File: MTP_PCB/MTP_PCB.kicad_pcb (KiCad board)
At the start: 2 copper layers, 65 x 56 mm, 21 parts, among them J1 GPIO, J2 USB_A, J3 Conn_01x03, SW1 SW_DPDT_x2, SW2 SW_DPDT_x2, SW3 SW_DPDT_x2, SW4 SW_DIP_x01, SW6 SW_DIP_x01, U1 NRF24L01_Breakout

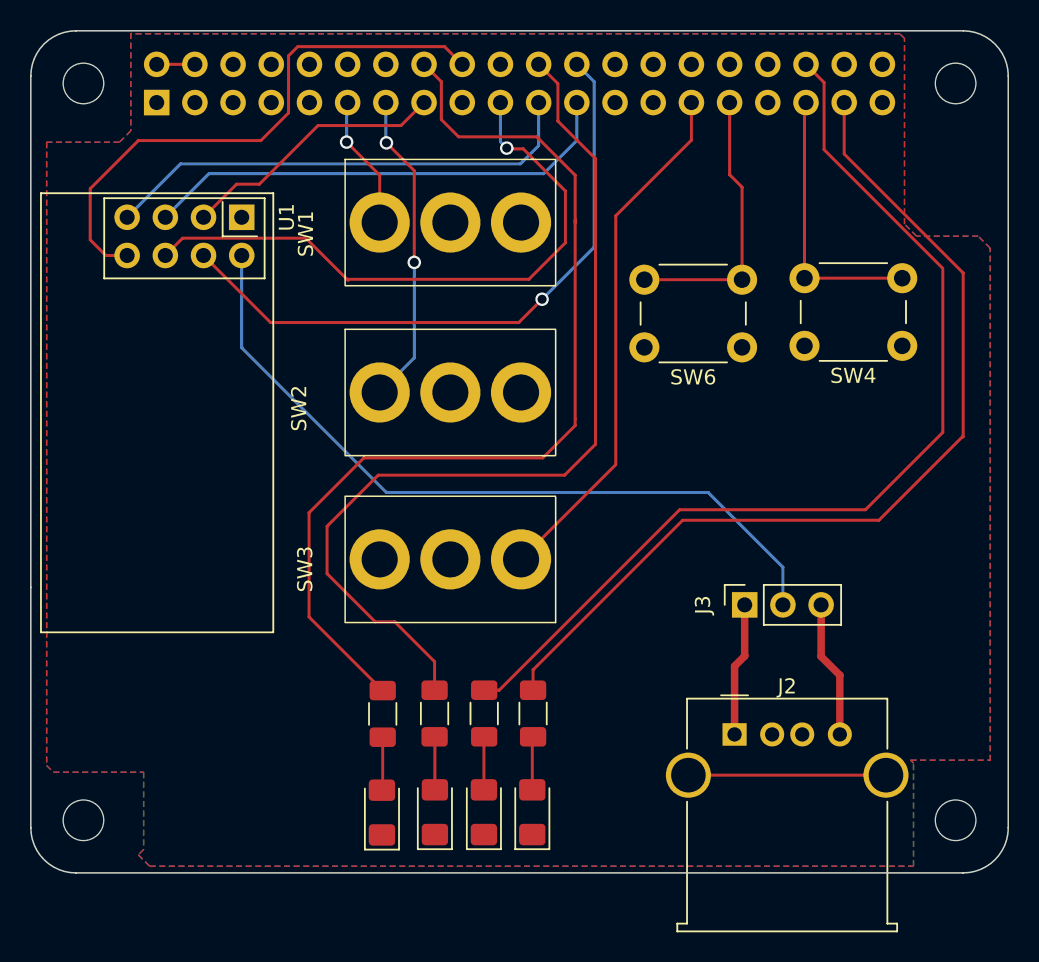
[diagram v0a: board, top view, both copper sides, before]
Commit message: remove GND planes
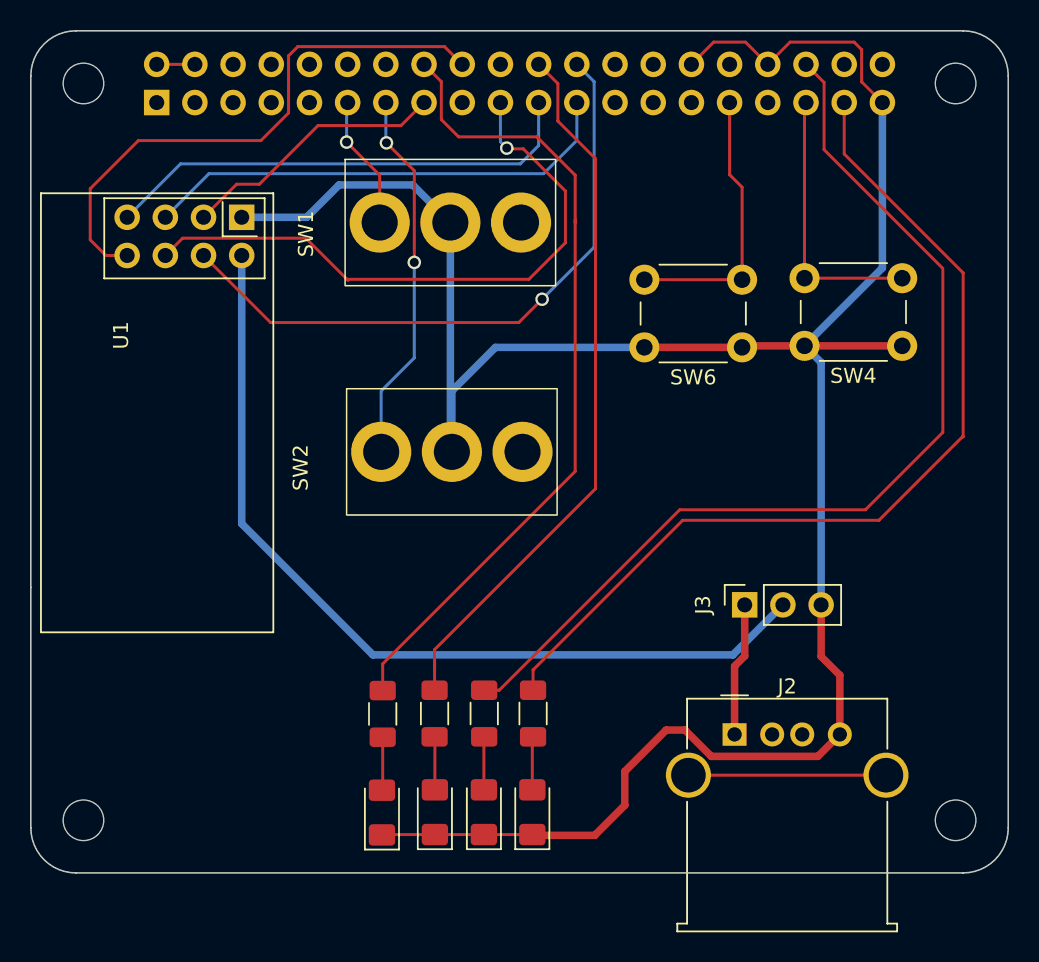
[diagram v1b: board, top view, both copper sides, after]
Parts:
- removed SW3: SW_DPDT_x2, MMS_footprints:SW_MTS102_3Pins_2Positions
- moved SW2 3.95 mm to (128.0, 72.0)
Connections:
- J2 pad 1: +5VA -> +5V
- J3 pad 1: +5VA -> +5V
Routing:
- net GND: track 9.13 -> 165.0 mm
- net /GPIO5: track 35.1 -> 0.00 mm
- net /GPIO25: track 61.6 -> 48.2 mm
- net /GPIO23: track 65.4 -> 54.4 mm
- net +5VA: track 8.89 -> 0.00 mm
- net +5V: track 2.54 -> 11.4 mm
- net +3.3VA: track 50.7 -> 58.8 mm
- net /GPIO27: track 21.0 -> 24.9 mm
- removed copper zone on B.Cu, net GND
- removed copper zone on F.Cu, net GND
